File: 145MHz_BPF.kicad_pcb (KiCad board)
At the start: 2 copper layers, 40 x 50 mm, 8 parts, among them J1 Conn_01x02_Socket, J2 Conn_01x02_Socket, J3 Conn_01x01_Socket, U1 SXBP-140

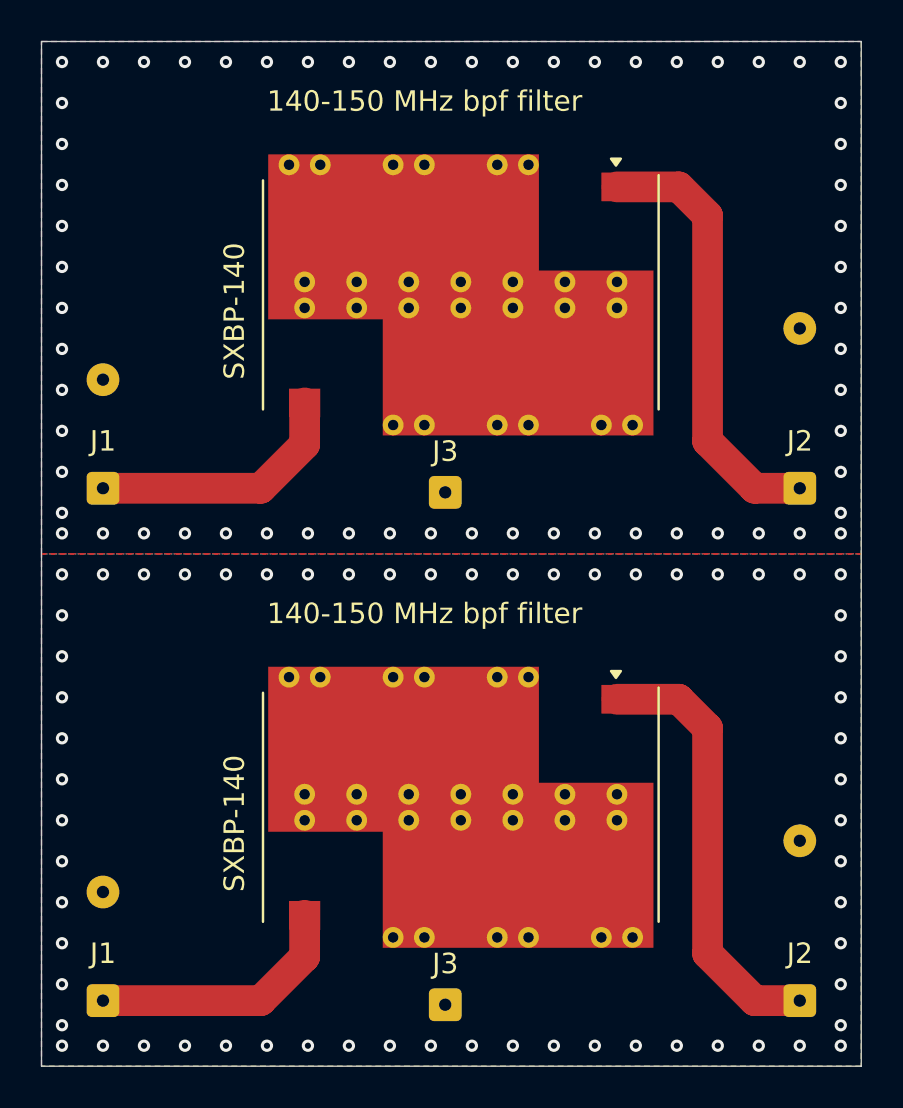
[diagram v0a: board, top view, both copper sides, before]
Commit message: 3D module added, error in gnd strap fixed
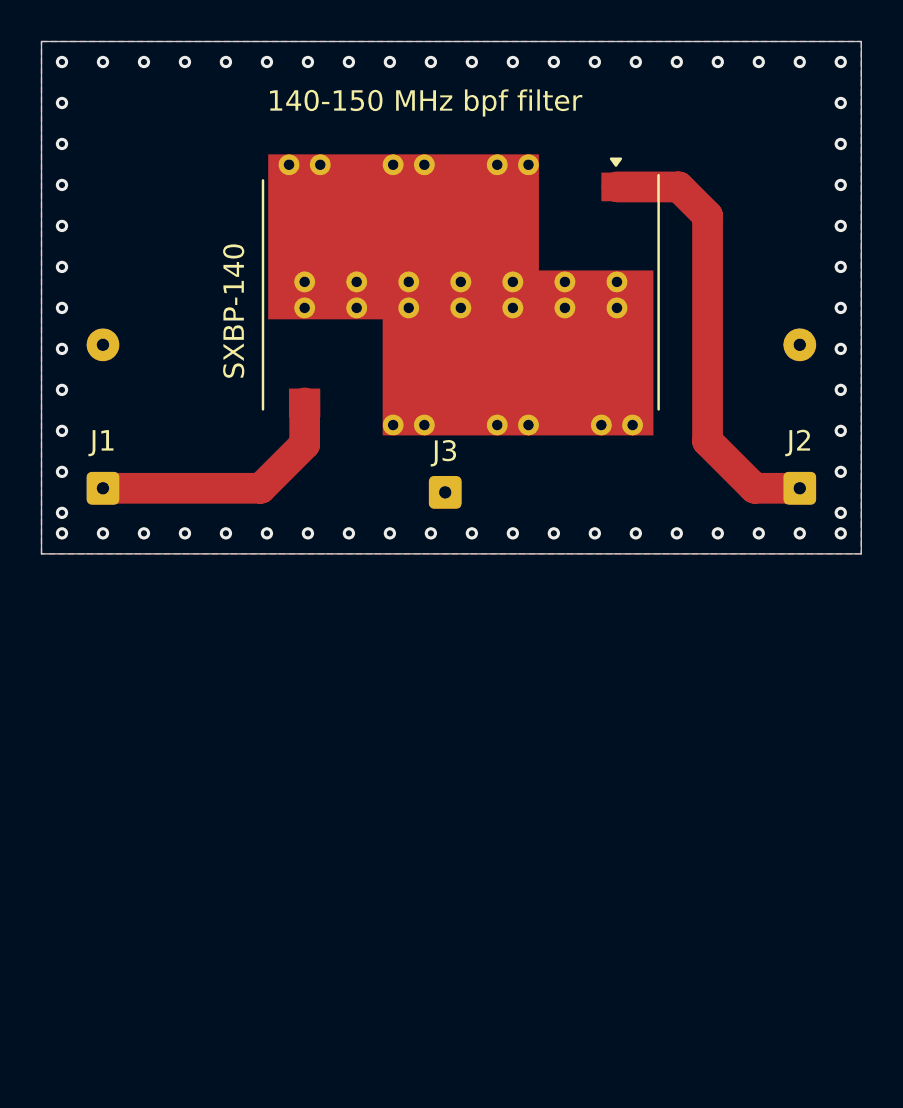
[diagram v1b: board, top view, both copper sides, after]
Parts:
- removed the J1 at (88.0, 91.8)
- removed the J2 at (122.0, 91.8)
- removed the J3 at (104.7, 92.0)
- removed the U1 at (105.5, 82.4)
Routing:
- net Net-(J2-Pin_1): track 42.9 -> 21.5 mm
- net Net-(J1-Pin_1): track 25.5 -> 12.8 mm
- net GND: vias 124 -> 62
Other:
- board size 40 x 50 mm -> 40 x 25 mm

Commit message: final release, Gerber ok
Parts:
- U1: value SXBP-140 -> SXBP-150
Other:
- board text added: "SXBP-150"
- board text removed: "SXBP-140"
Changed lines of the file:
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@@
 			(plot_on_all_layers_selection 0x0000000_00000000)
 			(disableapertmacros no)
-			(usegerberextensions no)
-			(usegerberattributes yes)
-			(usegerberadvancedattributes yes)
-			(creategerberjobfile yes)
+			(usegerberextensions yes)
+			(usegerberattributes no)
+			(usegerberadvancedattributes no)
+			(creategerberjobfile no)
 			(dashed_line_dash_ratio 12.000000)
 			(dashed_line_gap_ratio 3.000000)
@@
 			(psa4output no)
 			(plotreference yes)
-			(plotvalue yes)
+			(plotvalue no)
 			(plotfptext yes)
 			(plotinvisibletext no)
@@
 			(outputformat 1)
 			(mirror no)
-			(drillshape 1)
+			(drillshape 0)
 			(scaleselection 1)
-			(outputdirectory "")
+			(outputdirectory "../Gerber/")
 		)
 	)
@@
 			)
 		)
-		(property "Value" "SXBP-140"
+		(property "Value" "SXBP-150"
 			(at 0 10.922 90)
 			(layer "F.Fab")
@@
 			(at 0 0 90)
 			(size 1.6 1.6)
-			(drill 0.6)
+			(drill 0.9)
 			(layers "*.Cu" "*.Mask")
 			(remove_unused_layers no)
@@
 			(at 7 0 90)
 			(size 1.6 1.6)
-			(drill 0.6)
+			(drill 0.9)
 			(layers "*.Cu" "*.Mask")
 			(remove_unused_layers no)
@@
 			(at 0 0)
 			(size 1.6 1.6)
-			(drill 0.6)
+			(drill 0.9)
 			(layers "*.Cu" "*.Mask")
 			(remove_unused_layers no)
@@
 			(at 0 0 90)
 			(size 1.6 1.6)
-			(drill 0.6)
+			(drill 0.9)
 			(layers "*.Cu" "*.Mask")
 			(remove_unused_layers no)
@@
 			(at 7 0 90)
 			(size 1.6 1.6)
-			(drill 0.6)
+			(drill 0.9)
 			(layers "*.Cu" "*.Mask")
 			(remove_unused_layers no)
@@
 		(layer "Edge.Cuts")
 	)
-	(gr_text "SXBP-140"
+	(gr_text "SXBP-150"
 		(at 95 61.5 90)
 		(layer "F.SilkS")

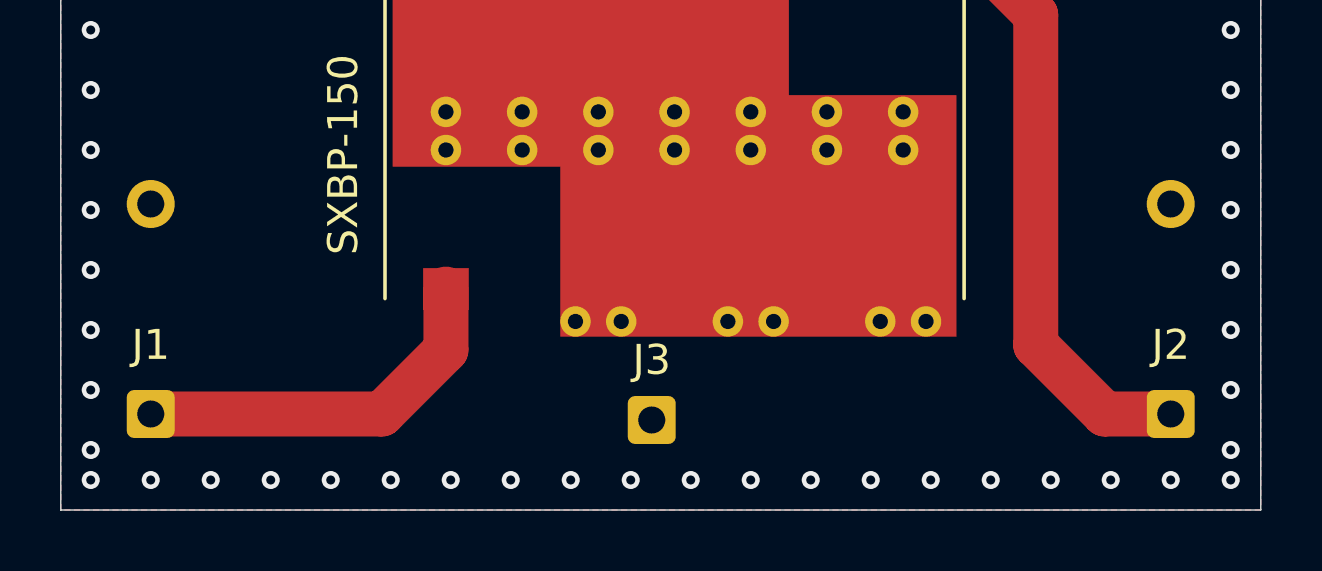
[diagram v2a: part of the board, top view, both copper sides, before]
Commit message: mmcx connector footprint added
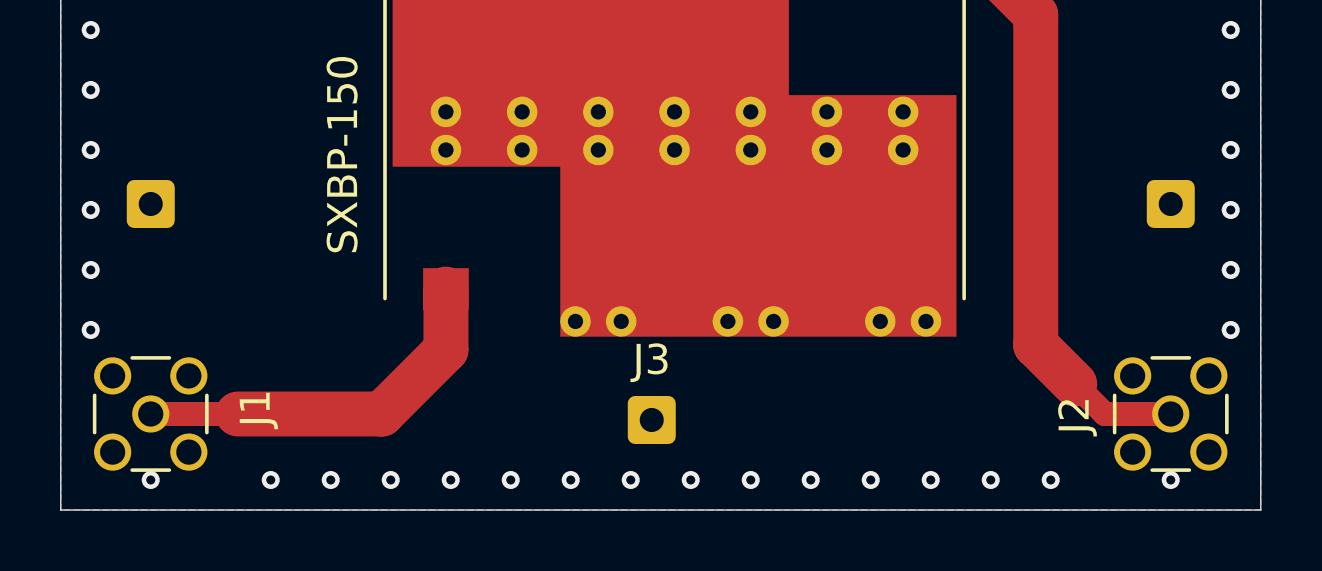
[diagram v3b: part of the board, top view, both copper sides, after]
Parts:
- added J4: Conn_01x01_Socket, Connector_Wire:SolderWire-0.1sqmm_1x01_D0.4mm_OD1mm, F.Cu at (71.1, 56.0)
- added J5: Conn_01x01_Socket, Connector_Wire:SolderWire-0.1sqmm_1x01_D0.4mm_OD1mm, F.Cu at (71.1, 59.7)
- J1, J2: footprint Connector_Wire:SolderWire-0.1sqmm_1x02_P3.6mm_D0.4mm_OD1mm -> Connector_Coaxial:MMCX_Molex_73415-1471_Vertical
- U1: value SXBP-150 -> SXBP-140
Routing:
- net Net-(J1-Pin_1): track 12.8 -> 12.2 mm
- net GND: vias 62 -> 54
